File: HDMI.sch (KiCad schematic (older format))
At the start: 6 parts, among them U1 RClamp0524PA, U2 RClamp0524PA, U3 HDMI_19plug_type_A, U4 RClamp0524PA

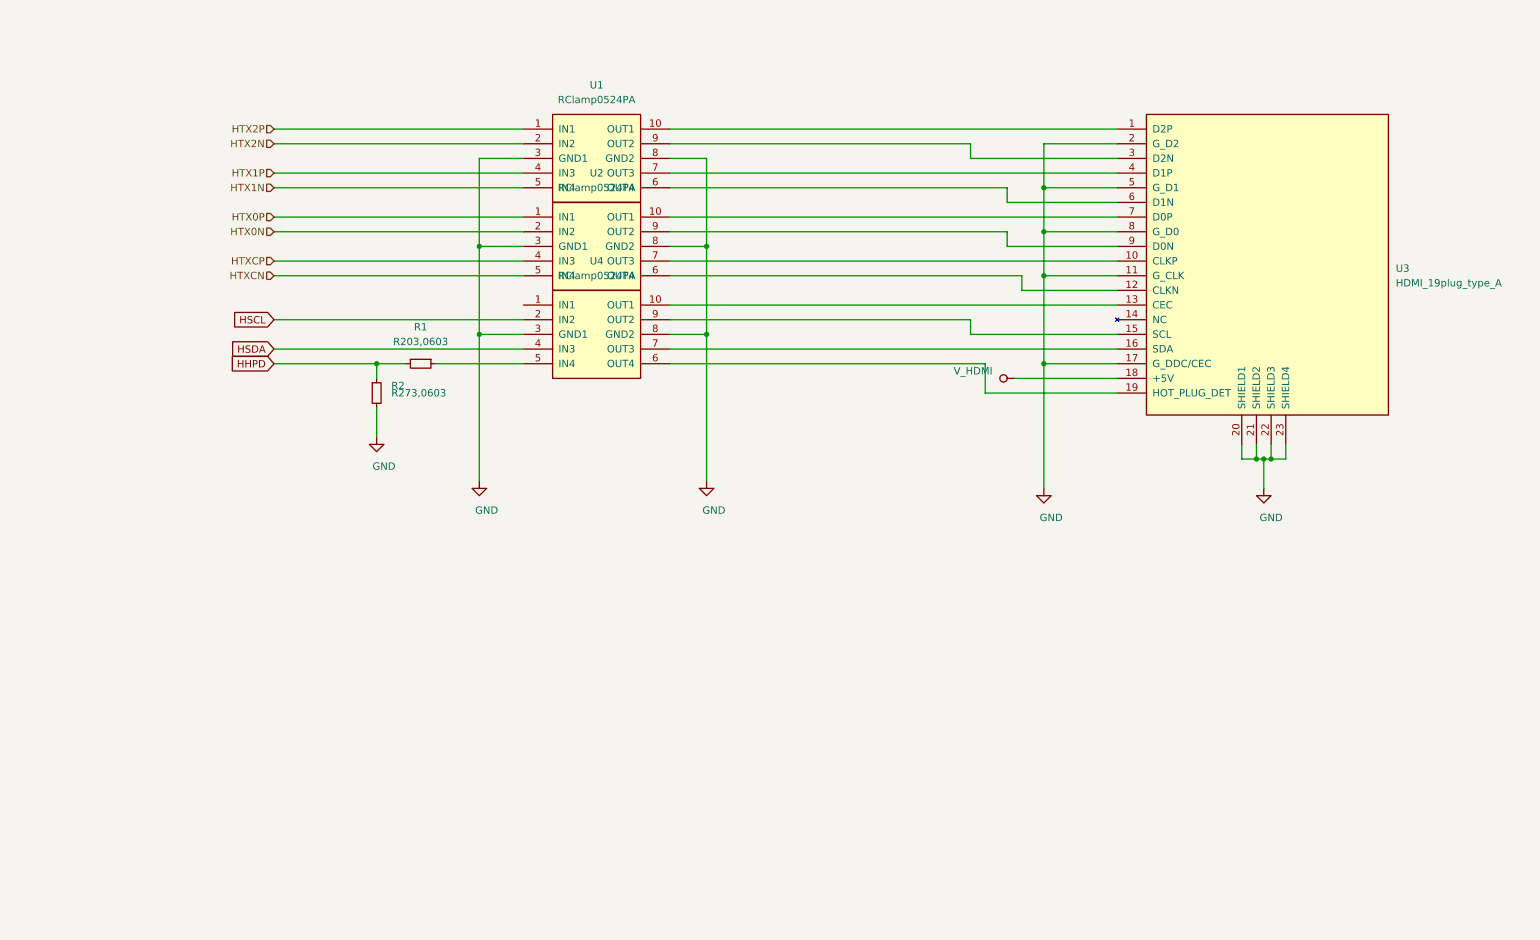
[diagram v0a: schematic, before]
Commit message: update HDMI,
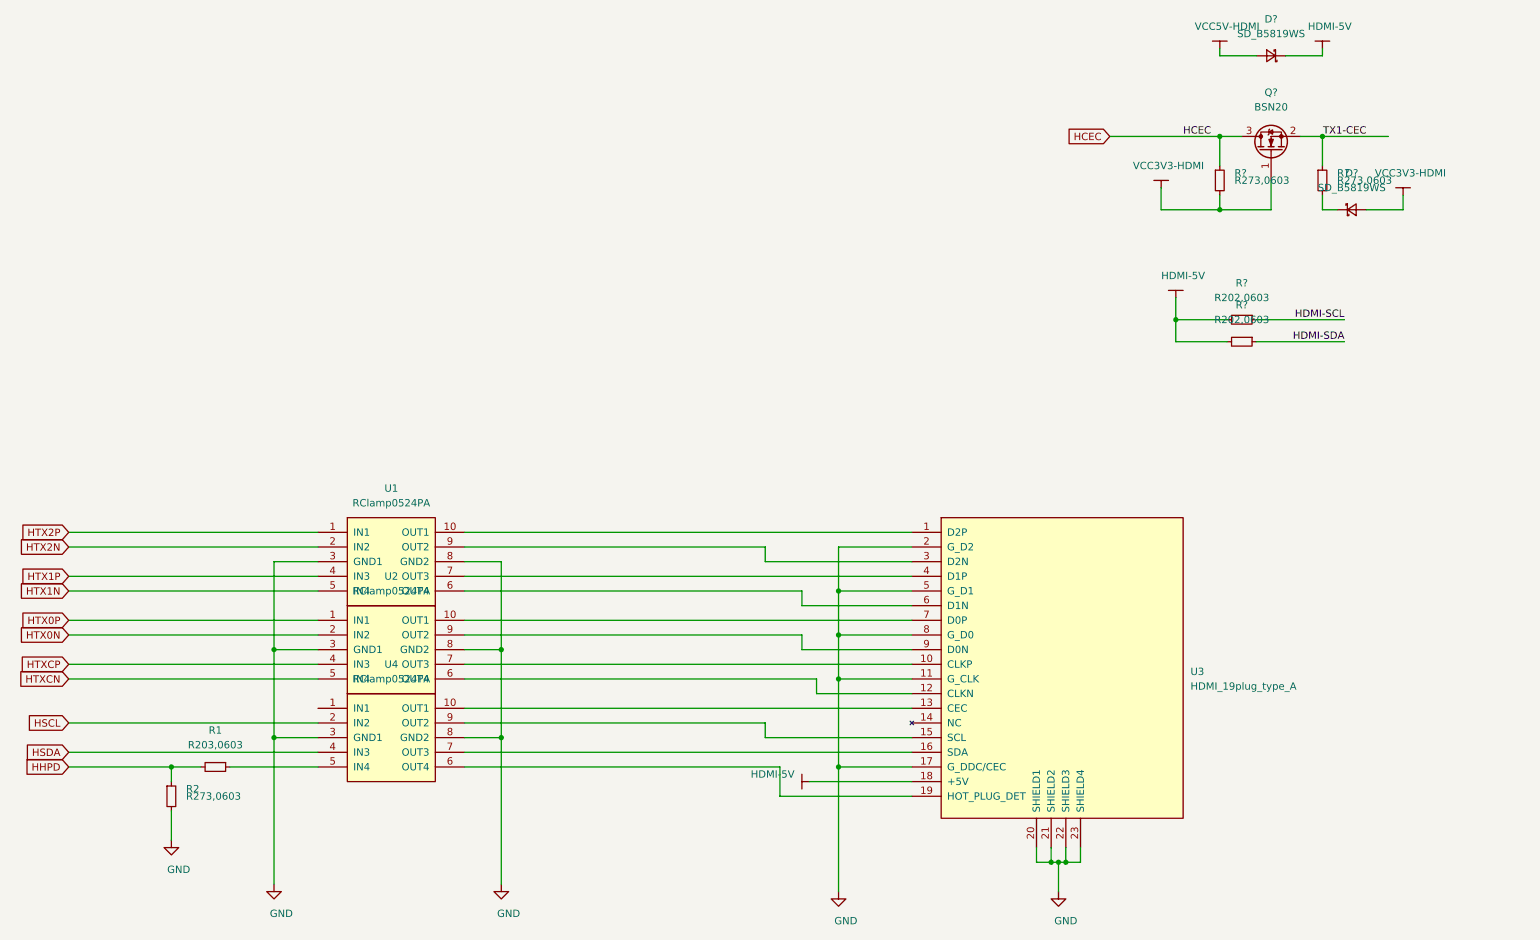
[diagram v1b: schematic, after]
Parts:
- added D? (x2): SD_B5819WS, symbol taobao-sd:SD_B5819WS
- added Q?: BSN20, symbol taobao-components:BSN20
- added R? (x2): R273,0603, Resistor_SMD:R_0603_1608Metric_Pad1.05x0.95mm_HandSolder, symbol taobao-r:R273,0603
- added R? (x2): R202,0603, Resistor_SMD:R_0603_1608Metric_Pad1.05x0.95mm_HandSolder, symbol taobao-r:R202,0603
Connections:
- net V_HDMI renamed HDMI-5V
- net HDMI-5V: now also D?.1 (K), R?.2, R?.2
- new net: D?.1 (K), R?.2
- new net HCEC: Q?.3 (D), R?.1
- new net HDMI-SCL: R?.1
- new net HDMI-SDA: R?.1
- new net TX1-CEC: Q?.2 (S), R?.1
- new net VCC3V3-HDMI: D?.2 (A), Q?.1 (G), R?.2
- new net VCC5V-HDMI: D?.2 (A)
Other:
- moved on the sheet: R1, R2, U1, U2, U3, U4

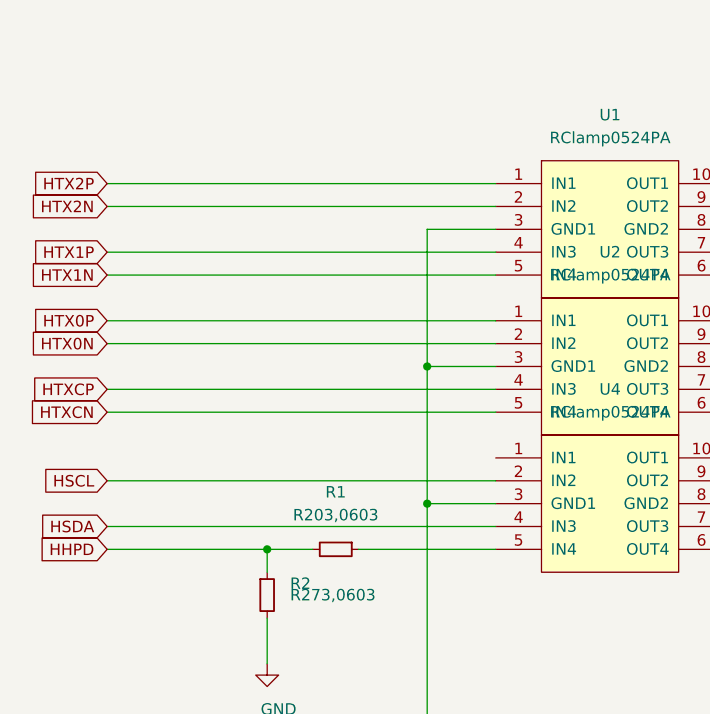
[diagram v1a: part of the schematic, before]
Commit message: update HDMI,
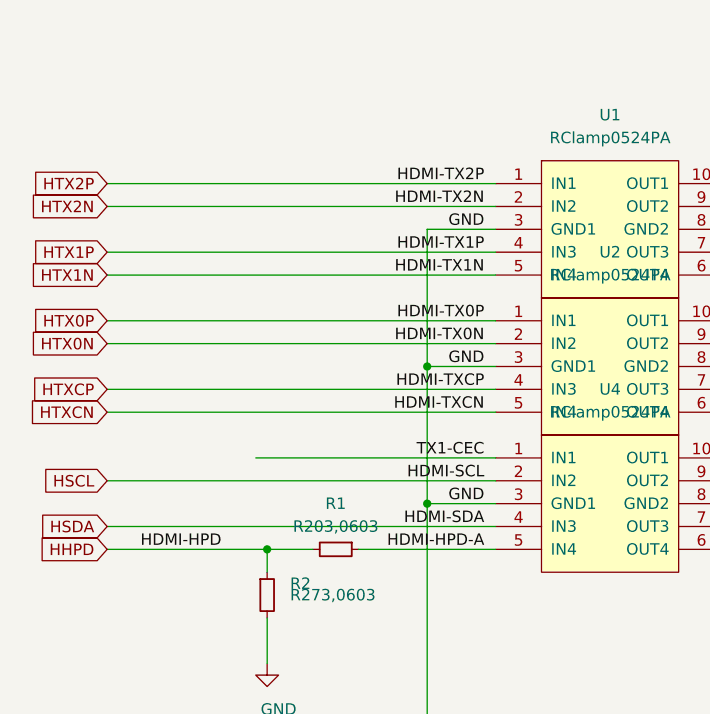
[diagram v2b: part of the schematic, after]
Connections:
- net HDMI-SCL is gone; now on net HSCL: R?.1
- net HDMI-SDA is gone; now on net HSDA: R?.1
- net TX1-CEC: now also U4.1 (IN1)
- net HDMI-HPD-A: now reaches R1.1, U4.5 (IN4)
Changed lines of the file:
@@
 AR Path="/5C1FD862/5C201210" Ref="R?"  Part="1"
 AR Path="/5C259FA6/5C201210" Ref="R?"  Part="1"
-F 0 "R1" V 1900 6450 50  0000 C CNN
-F 1 "R203,0603" V 2000 6450 50  0000 C CNN
+F 0 "R1" V 1950 6450 50  0000 C CNN
+F 1 "R203,0603" V 2050 6450 50  0000 C CNN
 F 2 "Resistor_SMD:R_0603_1608Metric_Pad1.05x0.95mm_HandSolder" H 2150 6450 50  0001 C CNN
 F 3 "~" H 2150 6450 50  0001 C CNN
@@
 Text GLabel 1150 5850 0    50   Input ~ 0
 HTXCN
+Text Label 2800 4850 2    50   ~ 0
+HDMI-TX2P
+Text Label 2800 4950 2    50   ~ 0
+HDMI-TX2N
+Text Label 2800 5050 2    50   ~ 0
+GND
+Text Label 2800 5150 2    50   ~ 0
+HDMI-TX1P
+Text Label 2800 5250 2    50   ~ 0
+HDMI-TX1N
+Text Label 2800 5450 2    50   ~ 0
+HDMI-TX0P
+Text Label 2800 5550 2    50   ~ 0
+HDMI-TX0N
+Text Label 2800 5650 2    50   ~ 0
+GND
+Text Label 2800 5750 2    50   ~ 0
+HDMI-TXCP
+Text Label 2800 5850 2    50   ~ 0
+HDMI-TXCN
+Text Label 2800 6050 2    50   ~ 0
+TX1-CEC
+Wire Wire Line
+	1800 6050 2850 6050
+Text Label 2800 6150 2    50   ~ 0
+HDMI-SCL
+Text Label 2800 6350 2    50   ~ 0
+HDMI-SDA
+Text Label 2800 6450 2    50   ~ 0
+HDMI-HPD-A
+Text Label 1650 6450 2    50   ~ 0
+HDMI-HPD
+Text Label 2800 6250 2    50   ~ 0
+GND
 $EndSCHEMATC
